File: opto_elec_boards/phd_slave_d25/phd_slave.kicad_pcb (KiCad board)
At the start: 2 copper layers, 63 x 95.2 mm, 20 parts, among them J1 From Main Board, M4a MountingHole_4.3mm_M4, M4b MountingHole_4.3mm_M4, M4c MountingHole_4.3mm_M4, M4d MountingHole_4.3mm_M4, U1 TL082, U2 OPA551

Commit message: Update OptoBoard / D25 version
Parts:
- removed J1: From Main Board, Connector_PinSocket_2.54mm:PinSocket_2x10_P2.54mm_Horizontal
- added J13: FromMainBoard, Connector_Dsub:DSUB-25_Socket_Horizontal_P2.77x2.84mm_EdgePinOffset7.70mm_Housed_MountingHolesOffset9.12mm, F.Cu at (58.4, 98.1)
- moved R6 39.5 mm to (123.2, 48.3), turned to -90 degrees
- moved M4c 34.1 mm to (129.5, 129.5)
- moved U1 24.5 mm to (71.1, 63.5)
- moved M4d 21.9 mm to (63.5, 116.8)
- moved R3 21.5 mm to (125.7, 100.3)
- moved G*** 21.4 mm to (61.0, 129.5)
- moved U2 18.8 mm to (71.1, 106.7), turned to 90 degrees
- moved M4b 18.7 mm to (129.5, 33.0)
- moved D6 15.3 mm to (125.7, 67.3)
- moved D3 15.0 mm to (125.7, 92.1)
- moved R5 14.3 mm to (108.0, 61.0)
- moved R2 12.6 mm to (110.5, 100.3)
- moved R4 12.0 mm to (92.7, 61.0), turned to 90 degrees
- moved D2 11.7 mm to (110.5, 92.1)
- moved D5 11.7 mm to (110.5, 67.3)
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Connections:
- D4 pad 1: +15V -> RVAR_15V
- D4 pad 2: OUT1 -> OUT3
- D5 pad 1: +15V -> RVAR_15V
- D6 pad 1: Net-(D6-K) -> RVAR_15V
- D6 pad 2: -15V -> Net-(D6-A)
- R4 pad 1: OUT1 -> OUT3
- R6 pad 1: OUT3 -> OUT1
- R6 pad 2: Net-(D6-K) -> Net-(D6-A)
- U1 pad 6: Net-(D6-K) -> Net-(D6-A)
- U1 pad 7: OUT3 -> OUT1
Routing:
- net +15V: track 206.3 -> 63.2 mm, vias 0 -> 1
- net RVAR_15V: track 0.00 -> 97.2 mm, vias 0 -> 1
- net Net-(D6-A): track 0.00 -> 63.8 mm
- net -15V: track 128.3 -> 71.2 mm, vias 0 -> 1
- net Net-(D6-K): track 54.2 -> 0.00 mm
- net OUT1: track 31.1 -> 83.9 mm
- net OUT2: track 53.1 -> 25.3 mm
- net OUT3: track 65.0 -> 51.1 mm, vias 1 -> 0
- net LED_IN: track 54.8 -> 68.0 mm
- net Net-(D5-A): track 32.9 -> 46.1 mm
- net OUT4: track 44.5 -> 54.9 mm, vias 1 -> 0
- net Net-(D2-K): track 3.56 -> 8.22 mm
- net IN1: track 55.9 -> 57.6 mm, vias 0 -> 2
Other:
- board size 63 x 95.2 mm -> 91.4 x 116.8 mm
- board text added: "+5V"
- board text added: "OUT4 -> U_Rled"
- board text added: "R_phd = 100 kO"
- board text added: "SEL1"
- board text removed: "+15V"
- board text removed: "IN1"

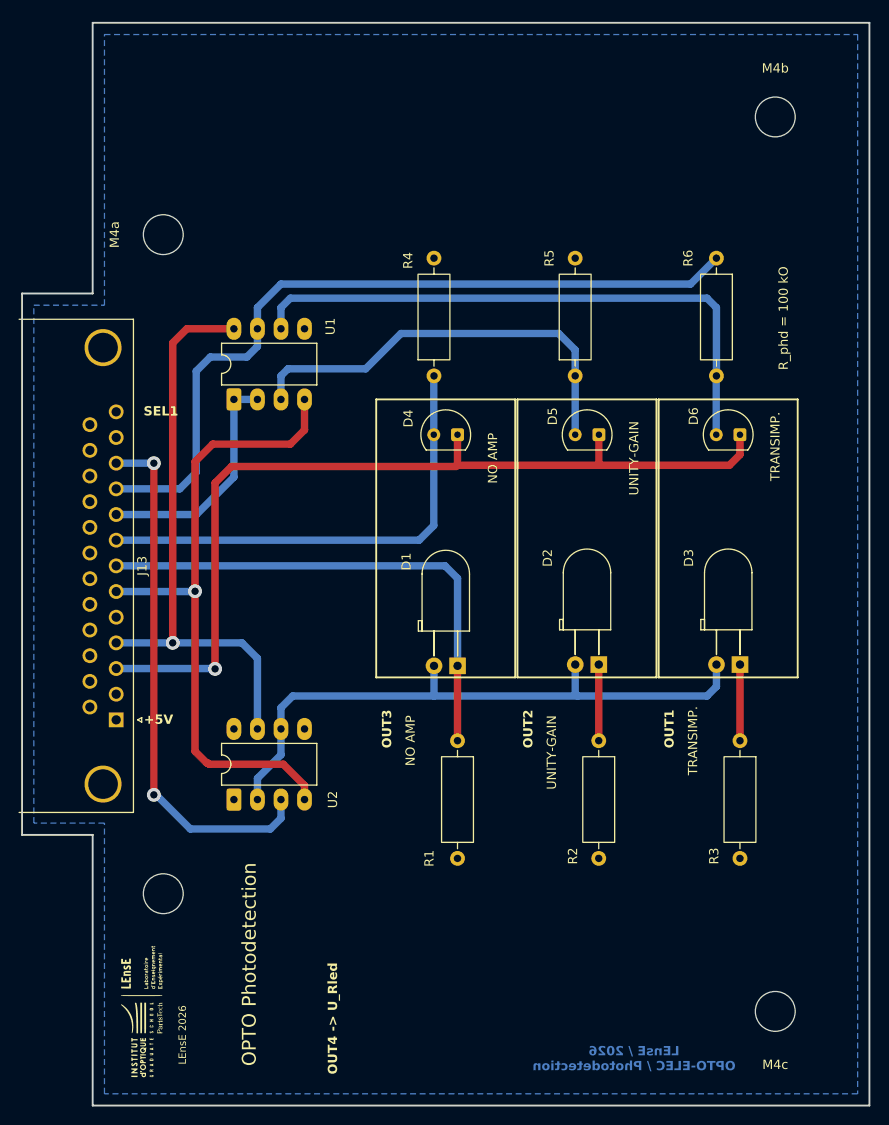
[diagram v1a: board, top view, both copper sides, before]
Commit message: Update Opto Board D25
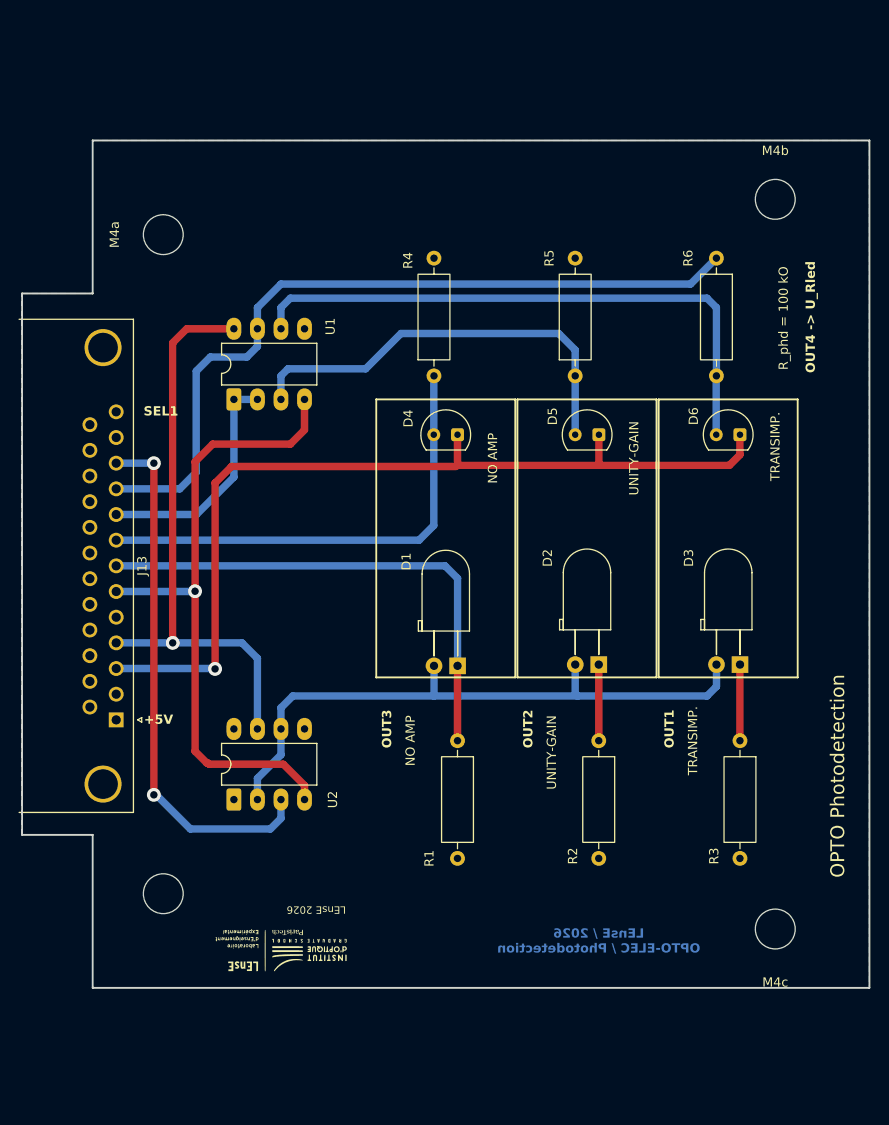
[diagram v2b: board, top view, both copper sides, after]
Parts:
- moved G*** 16.5 mm to (76.2, 123.2), turned to 180 degrees
- moved M4b 8.89 mm to (129.5, 41.9)
- moved M4c 8.89 mm to (129.5, 120.7)
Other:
- board size 91.4 x 116.8 mm -> 91.4 x 91.4 mm

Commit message: Update Opto D25
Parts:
- removed the G*** at (76.2, 123.2)
- added G***: LOGO, LEnsE_devices:Logo_New_Small, F.Cu at (77.0, 122.4)

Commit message: Update Opto / Master and PhD Slave boards
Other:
- board text removed: "R_phd = 100 kO"
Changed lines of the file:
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@@
 			(at -5.25 0 90)
 			(layer "F.SilkS")
+			(hide yes)
 			(effects
 				(font
@@
 			(at 0 5.75 0)
 			(layer "F.SilkS")
+			(hide yes)
 			(effects
 				(font
@@
 			(at 0 -5.25 0)
 			(layer "F.SilkS")
+			(hide yes)
 			(effects
 				(font
@@
 			)
 		)
-	)
-	(gr_text "R_phd = 100 kO"
-		(at 130.429 54.737 90)
-		(layer "F.SilkS")
-		(effects
-			(font
-				(size 1 1)
-				(thickness 0.125)
-			)
-		)

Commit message: Update Opto Boards / Phd_slave_d25 with CT for transimpedance
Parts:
- added J1: Conn_01x02, Connector_PinSocket_2.54mm:PinSocket_1x02_P2.54mm_Vertical, F.Cu at (129.0, 57.4)
- added J2: Conn_01x02, Connector_PinSocket_2.54mm:PinSocket_1x02_P2.54mm_Vertical, F.Cu at (129.0, 49.3)
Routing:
- net Net-(D6-A): track 63.8 -> 72.6 mm
- net OUT1: track 83.9 -> 92.7 mm
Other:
- board text added: "CT"
